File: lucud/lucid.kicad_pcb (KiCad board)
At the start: 2 copper layers, 2 parts, among them U1 STM32F373VCTx, U2 R-78E3.3-0.5

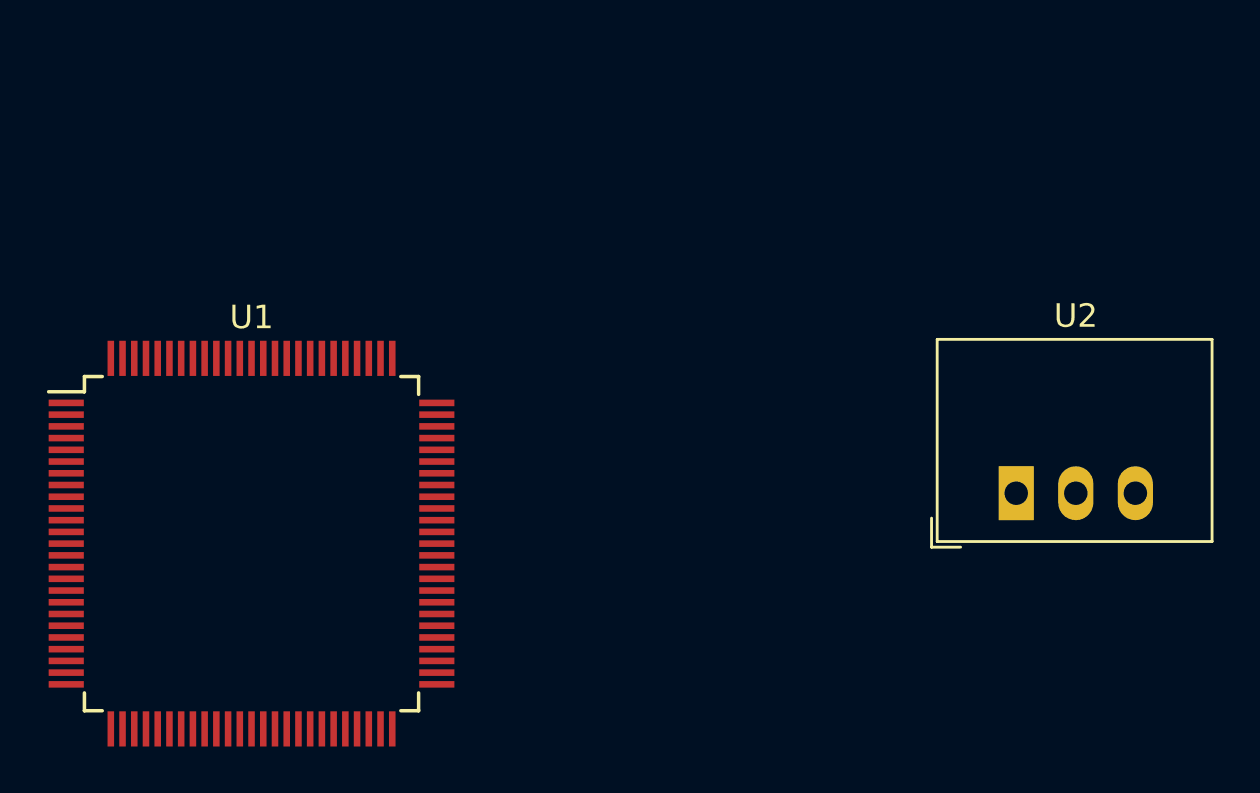
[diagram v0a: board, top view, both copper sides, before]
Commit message: Added power headers and some caps for the pcb.
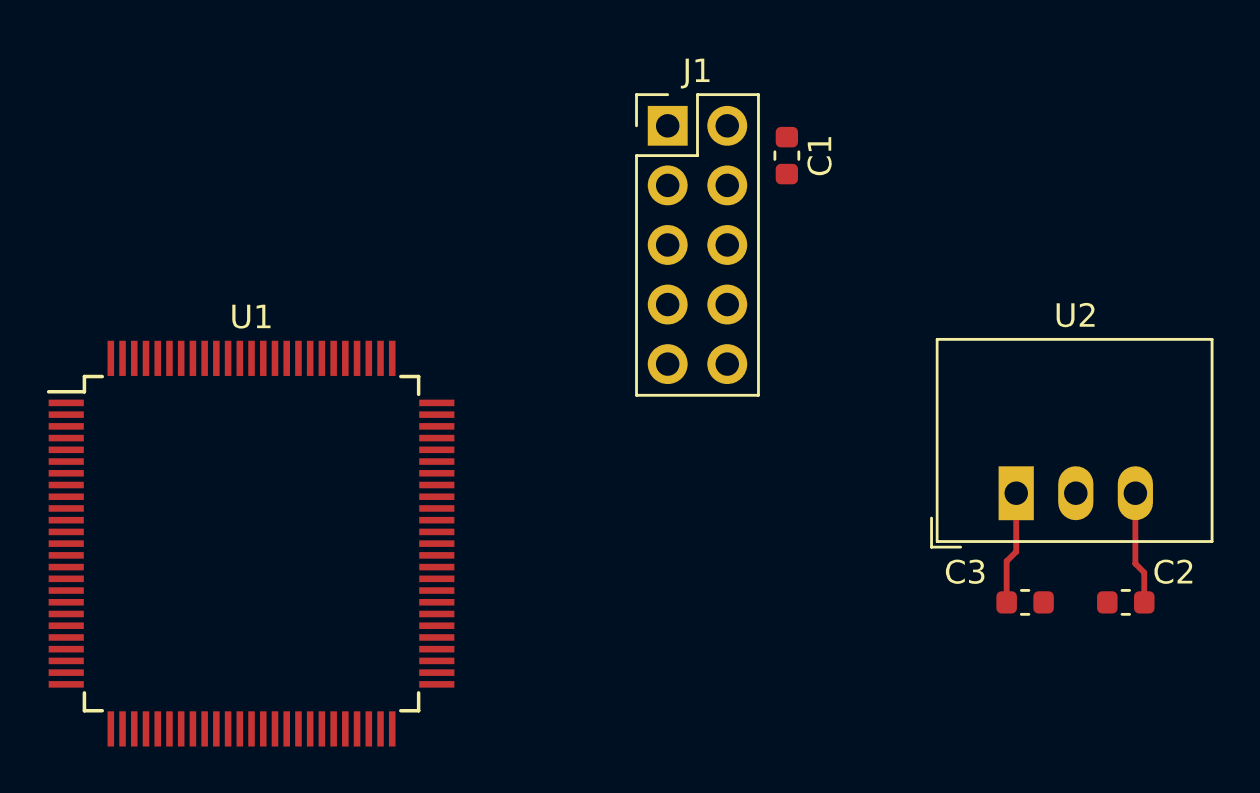
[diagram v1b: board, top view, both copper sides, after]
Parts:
- added C1: 1uF, Capacitor_SMD:C_0603_1608Metric, F.Cu at (147.3, 62.2)
- added C2: 1uF, Capacitor_SMD:C_0603_1608Metric, F.Cu at (161.8, 81.3)
- added C3: 1uF, Capacitor_SMD:C_0603_1608Metric, F.Cu at (157.5, 81.3)
- added J1: Conn_02x05_Odd_Even, Connector_PinHeader_2.54mm:PinHeader_2x05_P2.54mm_Vertical, F.Cu at (142.2, 61.0)
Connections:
- U2 pad 1: Net-(U2-Pad1) -> +12V
- U2 pad 2: Net-(U2-Pad2) -> GND
- U2 pad 3: Net-(U2-Pad3) -> +3V3
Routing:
- net +12V: track 0.00 -> 4.82 mm
- net +3V3: track 0.00 -> 4.81 mm
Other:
- copper layers 2 -> 4
